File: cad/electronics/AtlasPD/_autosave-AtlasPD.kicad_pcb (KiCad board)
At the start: 4 copper layers, 150.4 x 115.3 mm, 67 parts, among them J1 Conn_01x02_Male, J2 Conn_01x02_Male, J201 USB_C_Receptacle_USB2.0, J202 Conn_01x04, J301 Conn_01x06, J302 Conn_01x06, J401 Conn_01x04, SW201 SW_SPST, U201 CP2104, U202 ATmega328P-AU, U301 74LS08, U302 DRV8837C, U303 DRV8837C, U401 AMS1117-3.3, U402 LM2678T-ADJ_NOPB, Y201 CSTNE16M0V53-R0

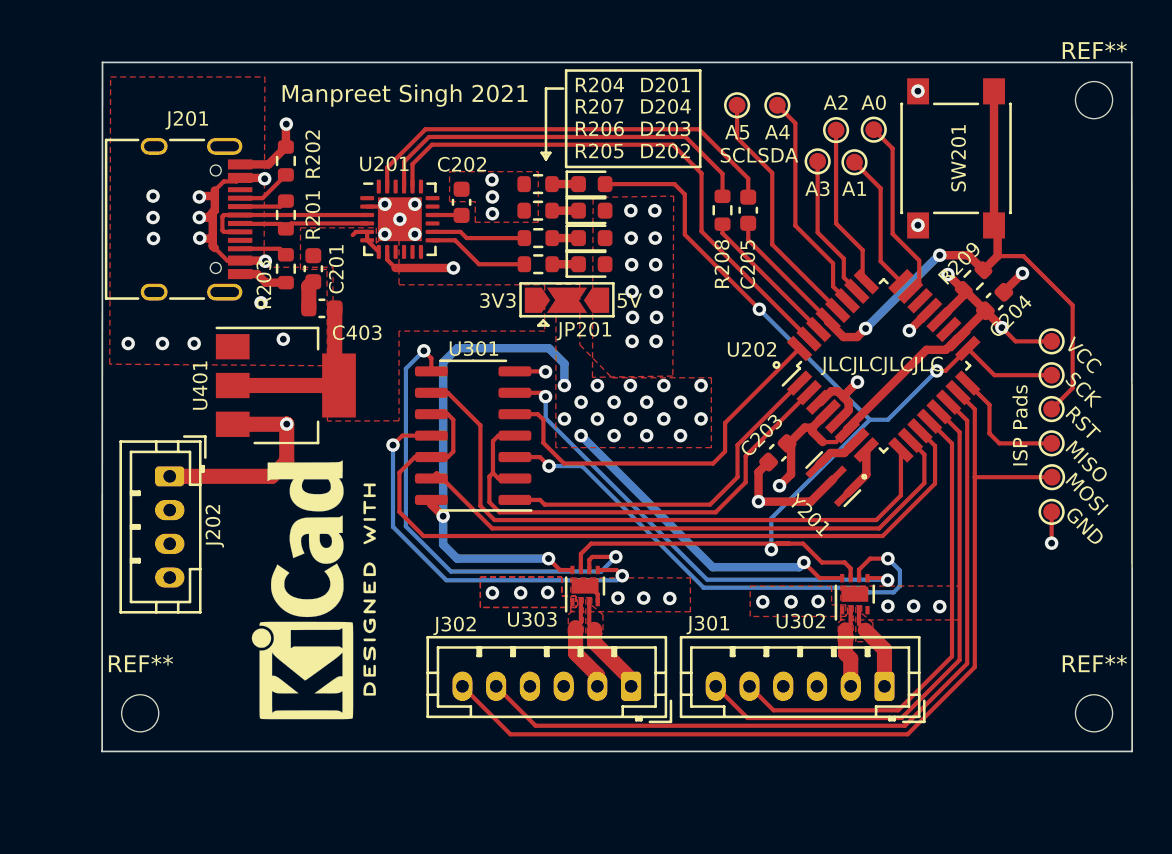
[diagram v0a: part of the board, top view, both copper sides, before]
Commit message: Small Layout Changes
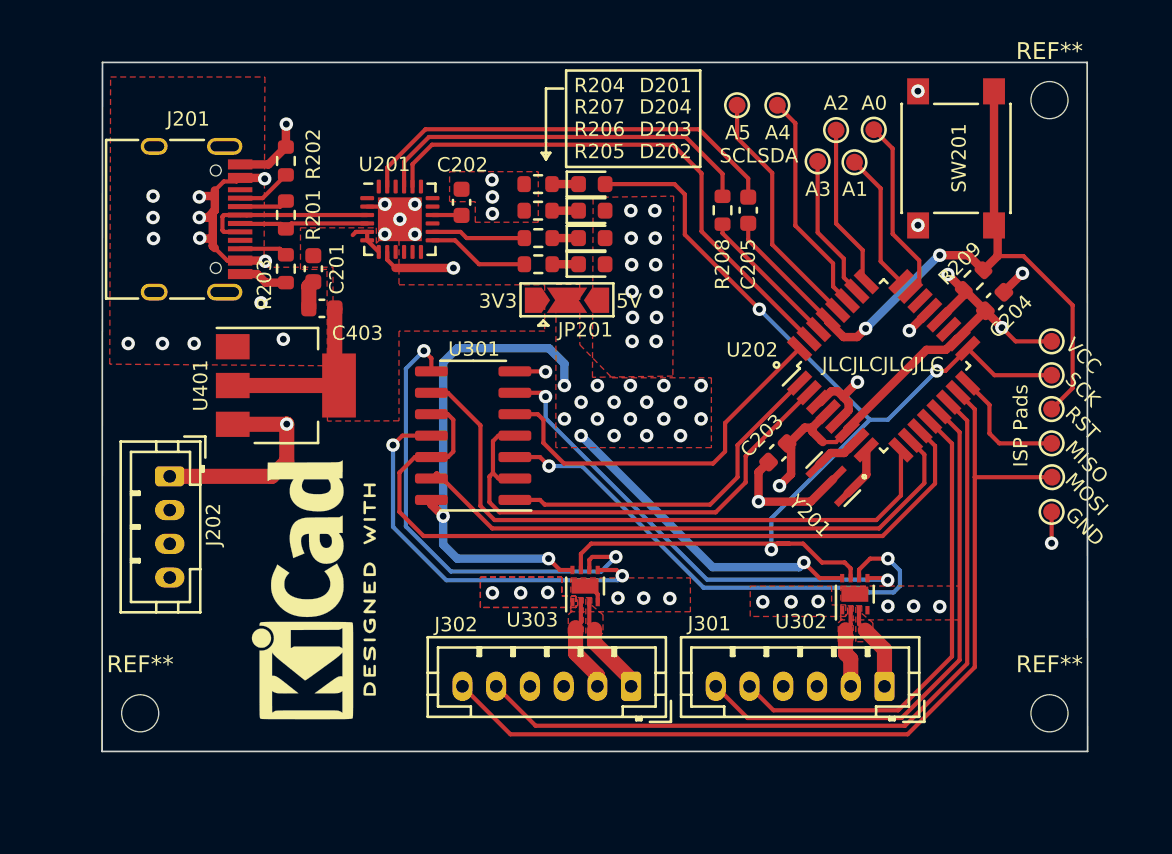
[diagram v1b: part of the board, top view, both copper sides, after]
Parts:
- added REF**: WEEE-Logo_8.4x12mm_SilkScreen, Symbol:WEEE-Logo_8.4x12mm_SilkScreen, B.Cu at (256.8, 55.8)
- moved REF** 2.64 mm to (256.7, 66.0)
- moved REF** 2.64 mm to (256.7, 29.6)
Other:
- board size 150.4 x 115.3 mm -> 147.8 x 115.3 mm

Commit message: Getting Ready to Fab MCU
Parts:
- removed the REF** at (256.8, 55.8)
- added REF**: ESD-Logo_6.6x6mm_SilkScreen, Symbol:ESD-Logo_6.6x6mm_SilkScreen, B.Cu at (212.3, 64.9)
- added REF**: WEEE-Logo_4.2x6mm_SilkScreen, Symbol:WEEE-Logo_4.2x6mm_SilkScreen, B.Cu at (217.5, 64.9)
- added REF**: MountingHole_2.2mm_M2_DIN965, MountingHole:MountingHole_2.2mm_M2_DIN965, F.Cu at (216.3, 29.6)
- REF**: moved to B.Cu
- moved REF** 35.5 mm to (242.0, 39.1), turned to 180 degrees
- moved TP208 5.41 mm to (255.2, 53.1)
- moved TP207 5.41 mm to (255.2, 59.2)
- moved TP209 5.41 mm to (255.2, 51.1)
- moved TP210 5.41 mm to (255.2, 55.1)
- moved TP212 5.41 mm to (255.2, 49.1)
- moved TP211 5.41 mm to (255.2, 57.1)
- moved J202 4.17 mm to (208.4, 53.5)
- moved C201 1.65 mm to (214.7, 39.6)
- moved J201 1.65 mm to (206.3, 36.7)
- moved R201 1.65 mm to (213.1, 36.4)
- moved R202 1.65 mm to (213.1, 33.2)
- moved R203 1.65 mm to (213.1, 39.6)
- moved C403 1.65 mm to (215.2, 42.0)
- moved U401 1.35 mm to (212.8, 46.6)
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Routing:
- net +BATT: track 0.00 -> 35.8 mm, vias 6 -> 12
- net +5V: track 90.8 -> 80.4 mm, vias 19 -> 18
- net GND: track 34.8 -> 41.8 mm, vias 65 -> 69
- net /Sheet60A2E58A/RESET: track 43.2 -> 48.7 mm
- net /Motor Driver/EN: track 65.7 -> 69.8 mm
- net VCC: track 79.6 -> 83.1 mm
- net /Sheet60A2E58A/IO12_MISO: track 7.45 -> 10.8 mm
- net /Motor Driver/IN3: track 37.1 -> 39.4 mm
- net /Motor Driver/PWM_B: track 46.5 -> 48.8 mm
- net /Motor Driver/IN4: track 34.7 -> 36.5 mm
- net /Sheet60A2E58A/USB_DN: track 7.80 -> 6.15 mm
- net /Motor Driver/S4: track 54.5 -> 52.9 mm
- net +3V3: track 13.4 -> 14.9 mm
- net /Sheet60A2E58A/IO1: track 32.1 -> 33.5 mm
- net /Sheet60A2E58A/IO0: track 8.60 -> 9.72 mm
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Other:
- outline, holes or cut-outs redrawn
- rule trace_min: 0.2 -> 0
- board text added: "+BAT"
- board text added: "Atlas MCU Rev. 1.0"
